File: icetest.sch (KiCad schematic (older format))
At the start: 30 parts

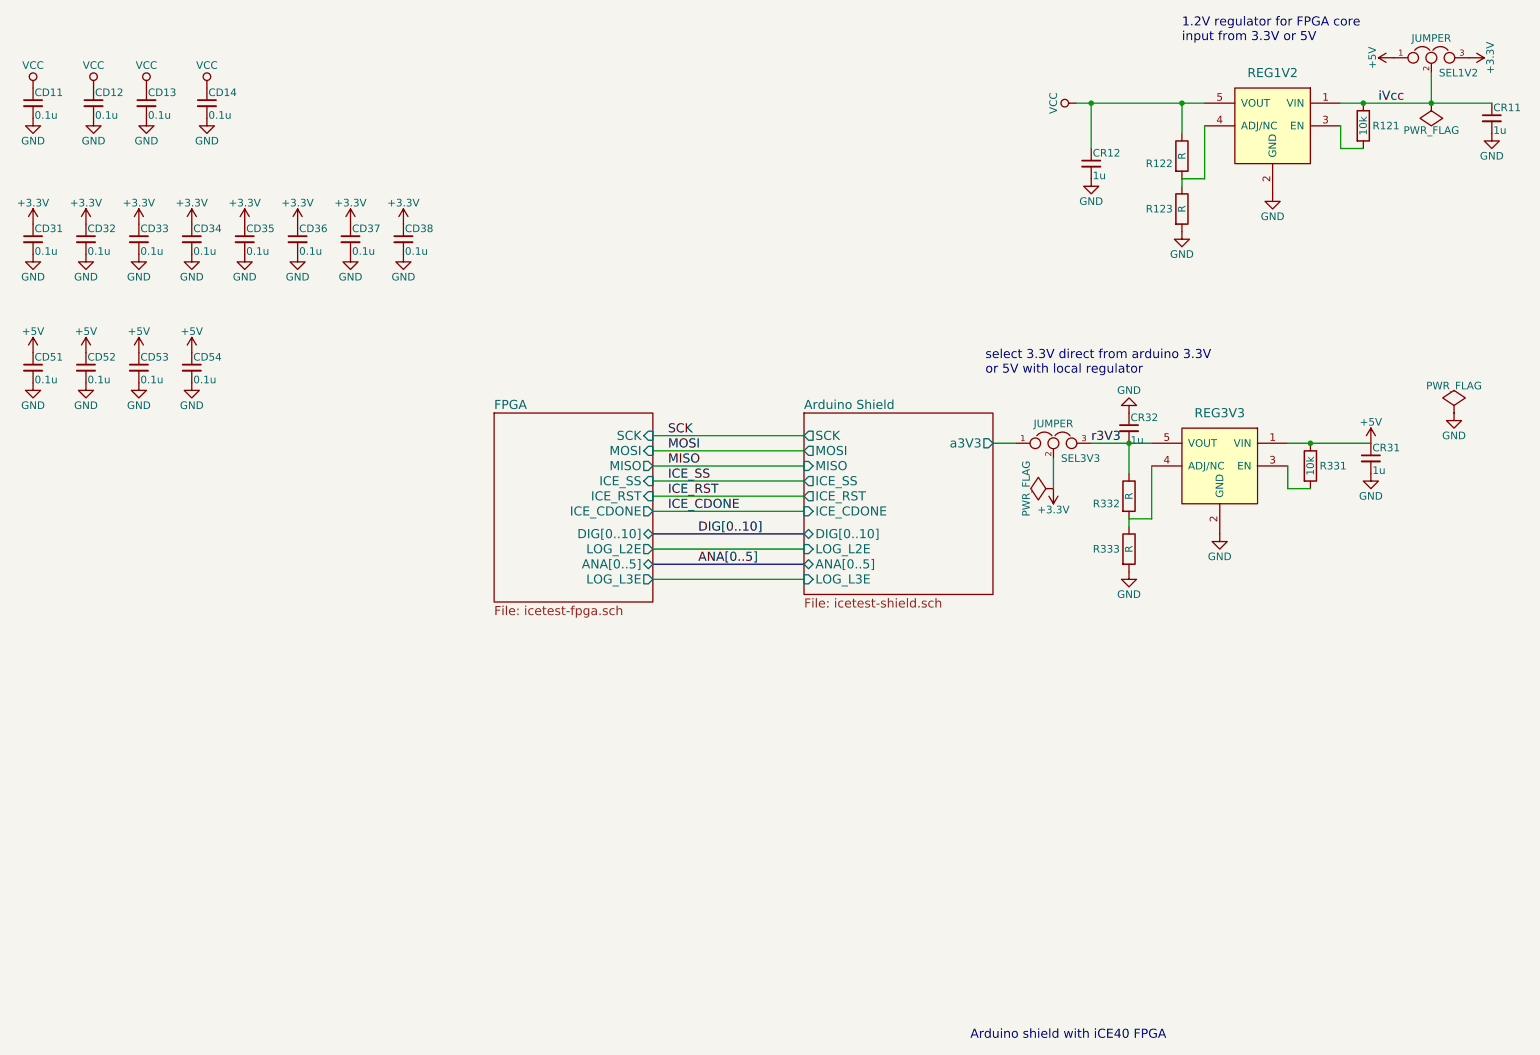
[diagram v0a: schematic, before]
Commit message: add SPI test points and verify footprints
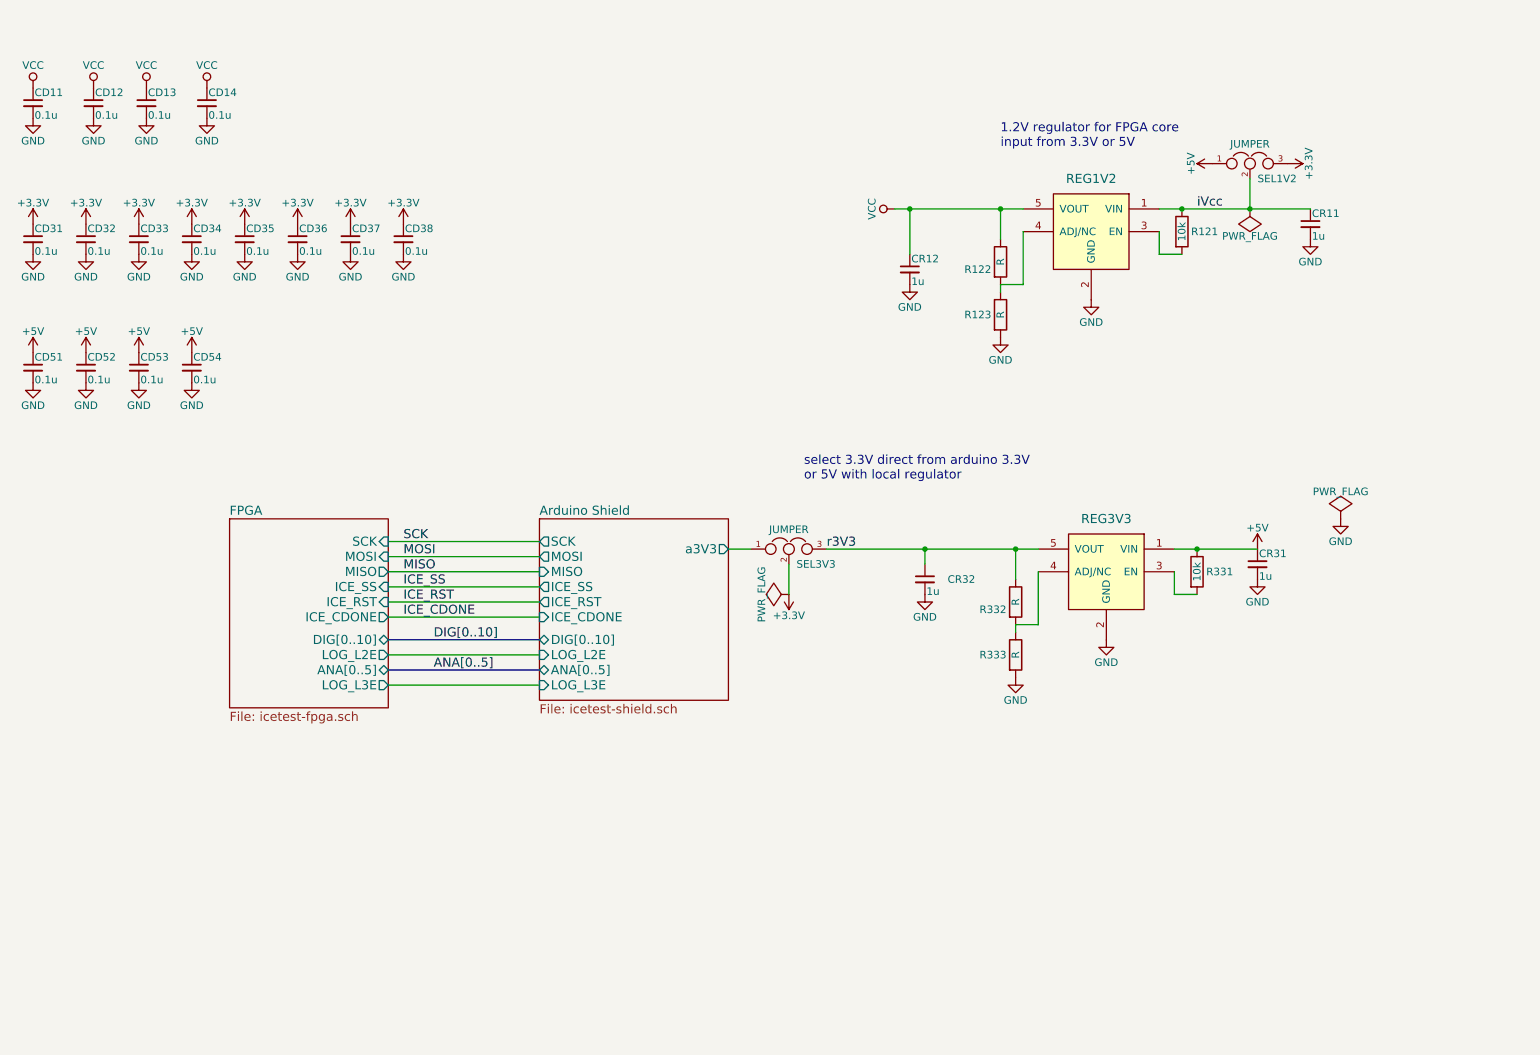
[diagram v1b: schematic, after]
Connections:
- net GND: now also CR32.2; no longer CR32.1
- net r3V3: now also CR32.1; no longer CR32.2
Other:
- note removed: "Arduino shield with iCE40 FPGA"
- moved on the sheet: CR11, CR12, CR31, R121, R122, R123, R331, R332, R333, REG1V2, REG3V3, SEL1V2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

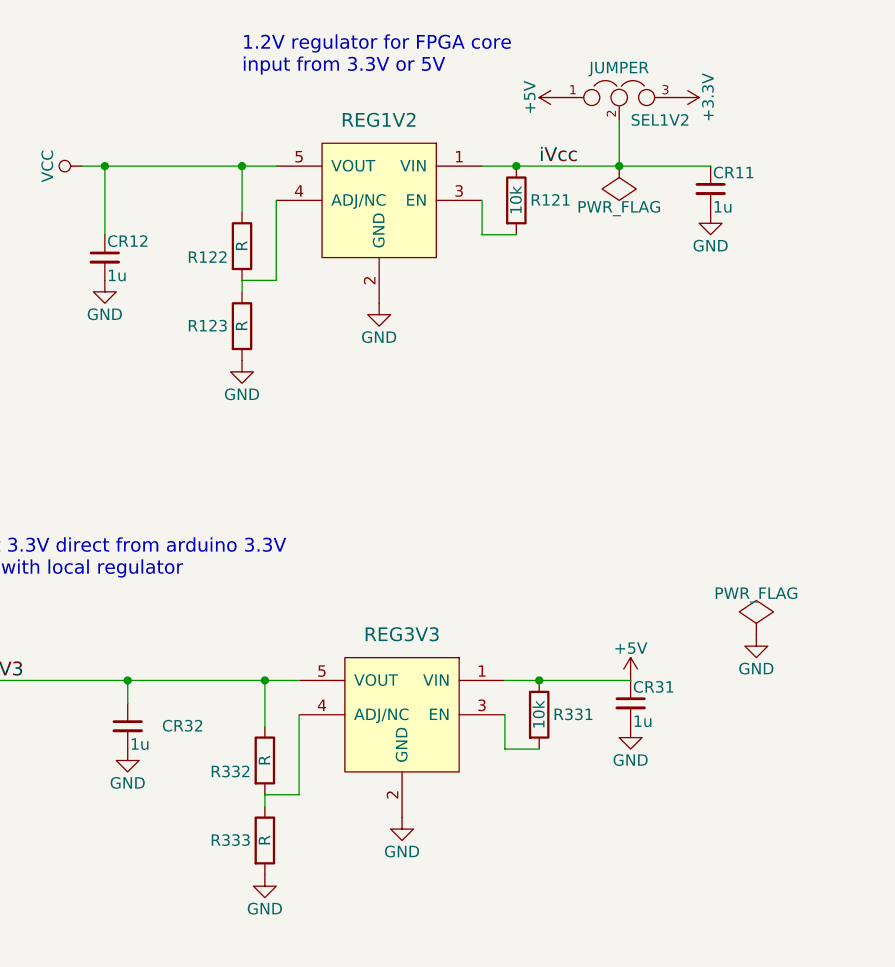
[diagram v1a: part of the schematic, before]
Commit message: fix schematic bugs
signal on N/C pin on ice40
1.2V regulator R divider moved to input side
Remove R divider for 3.3V (not needed for fixed V model)
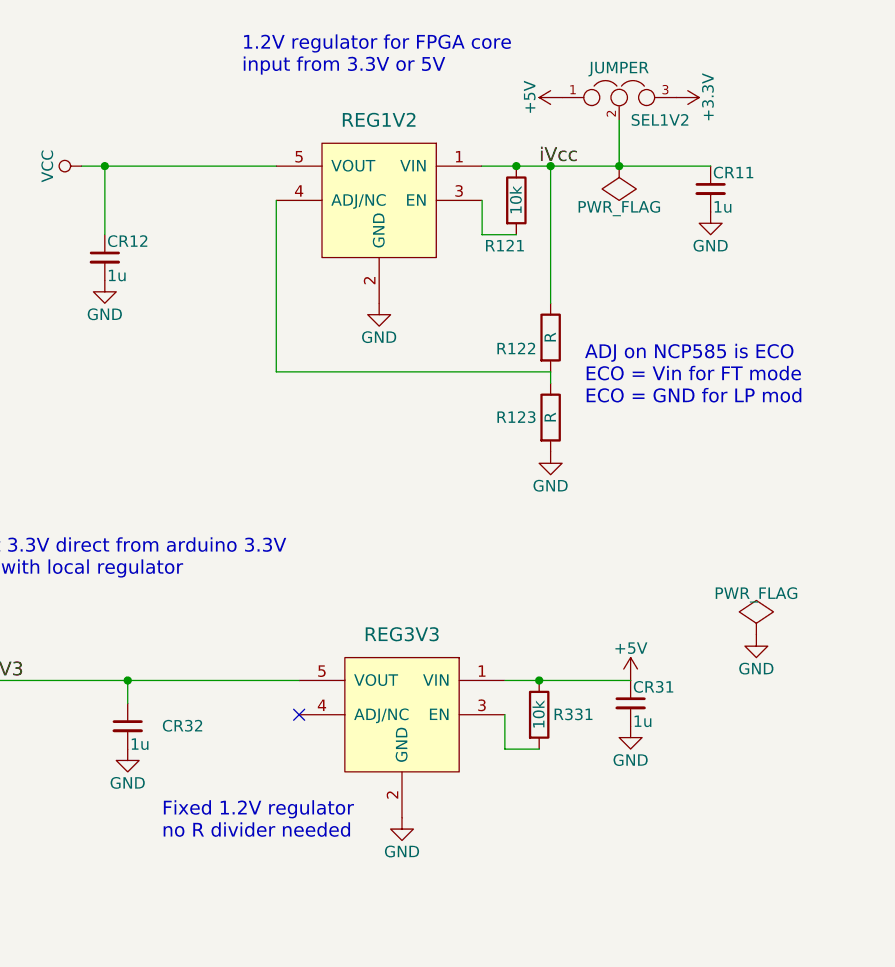
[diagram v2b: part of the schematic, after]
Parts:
- removed R332, R333: R, Resistors_SMD:R_0603_HandSoldering, symbol R
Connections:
- net VCC: no longer R122.1
- net iVcc: now also R122.1
- no-connect marks 0 -> 1
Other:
- note added: "ADJ on NCP585 is ECO\nECO = Vin for FT mode\nECO = GND for LP mod"
- note added: "Fixed 1.2V regulator\nno R divider needed"
- moved on the sheet: R122, R123

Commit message: clean and oshpart rules
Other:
- note added: "Both regulators have\nactive high enable"
- note added: "Fixed 3.3V regulator\nno R divider needed"
- note removed: "Fixed 1.2V regulator\nno R divider needed"
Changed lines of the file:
@@
 NoConn ~ 7850 4400
 Text Notes 7250 4950 0    60   ~ 0
-Fixed 1.2V regulator\nno R divider needed
+Fixed 3.3V regulator\nno R divider needed
+Text Notes 8450 3750 0    60   ~ 0
+Both regulators have\nactive high enable
 $EndSCHEMATC

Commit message: add schematic notes
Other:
- note added: "I/O interconnects\nas 3.3v"
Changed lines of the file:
@@
 Text Notes 8450 3750 0    60   ~ 0
 Both regulators have\nactive high enable
+Text Notes 3650 5550 0    60   ~ 0
+I/O interconnects\nas 3.3v
 $EndSCHEMATC

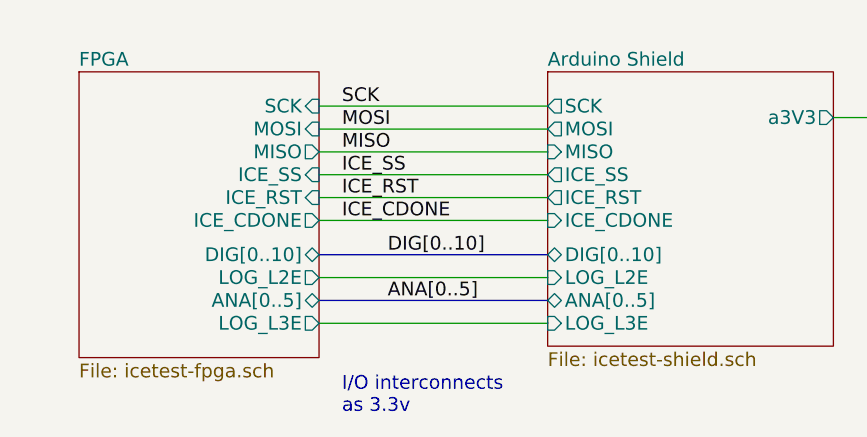
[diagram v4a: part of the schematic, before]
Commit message: switch level shifter
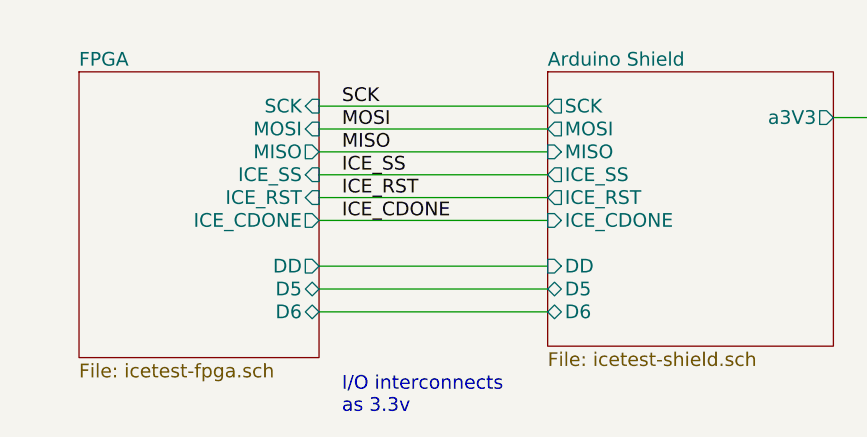
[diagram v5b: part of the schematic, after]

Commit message: redo layout
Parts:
- added W12: TEST_1P, Connect:PINTST, symbol TEST_1P
- SEL1V2, SEL3V3: footprint Connect:PINHEAD1-3 -> Pin_Headers:Pin_Header_Straight_1x03
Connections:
- net VCC: now also W12.1
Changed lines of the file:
@@
 Title "Arduino shield with iCE40 FPGA"
 Date ""
-Rev "0"
+Rev "2"
 Comp "mdavidsaver@gmail.com"
 Comment1 ""
@@
 F 0 "SEL3V3" H 6250 4150 50  0000 L CNN
 F 1 "JUMPER" H 6200 4350 50  0000 C BNN
-F 2 "Connect:PINHEAD1-3" H 6200 4250 50  0001 C CNN
+F 2 "Pin_Headers:Pin_Header_Straight_1x03" H 6200 4250 50  0001 C CNN
 F 3 "" H 6200 4250 50  0000 C CNN
 	1    6200 4250
@@
 F 0 "SEL1V2" H 9300 1600 50  0000 L CNN
 F 1 "JUMPER" H 9250 1800 50  0000 C BNN
-F 2 "Connect:PINHEAD1-3" H 9250 1700 50  0001 C CNN
+F 2 "Pin_Headers:Pin_Header_Straight_1x03" H 9250 1700 50  0001 C CNN
 F 3 "" H 9250 1700 50  0000 C CNN
 	1    9250 1700
@@
 Wire Wire Line
 	3550 5100 4550 5100
+$Comp
+L TEST_1P W12
+U 1 1 57FAF380
+P 7000 2000
+F 0 "W12" H 7000 2270 50  0000 C CNN
+F 1 "TEST_1P" H 7000 2200 50  0000 C CNN
+F 2 "Connect:PINTST" H 7200 2000 50  0001 C CNN
+F 3 "" H 7200 2000 50  0000 C CNN
+	1    7000 2000
+	1    0    0    -1
+$EndComp
 $EndSCHEMATC

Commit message: more layout
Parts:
- added CR4: 1u, Capacitors_SMD:C_0603_HandSoldering, symbol C_Small
- R122, R123: value R -> 10k
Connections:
- net Arduino Shield/a3V3: now also CR4.1
- net GND: now also CR4.2
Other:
- moved on the sheet: SEL3V3
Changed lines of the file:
@@
 L JUMPER3 SEL3V3
 U 1 1 578B8877
-P 6200 4250
-F 0 "SEL3V3" H 6250 4150 50  0000 L CNN
-F 1 "JUMPER" H 6200 4350 50  0000 C BNN
-F 2 "Pin_Headers:Pin_Header_Straight_1x03" H 6200 4250 50  0001 C CNN
-F 3 "" H 6200 4250 50  0000 C CNN
-	1    6200 4250
-	1    0    0    -1
-$EndComp
-Wire Wire Line
-	5950 4250 5800 4250
+P 6500 4250
+F 0 "SEL3V3" H 6550 4150 50  0000 L CNN
+F 1 "JUMPER" H 6500 4350 50  0000 C BNN
+F 2 "Pin_Headers:Pin_Header_Straight_1x03" H 6500 4250 50  0001 C CNN
+F 3 "" H 6500 4250 50  0000 C CNN
+	1    6500 4250
+	1    0    0    -1
+$EndComp
+Wire Wire Line
+	6250 4250 5800 4250
 $Comp
 L +3.3V #PWR01
 U 1 1 578B8957
-P 6200 4550
-F 0 "#PWR01" H 6200 4400 50  0001 C CNN
-F 1 "+3.3V" H 6200 4690 50  0000 C CNN
-F 2 "" H 6200 4550 50  0000 C CNN
-F 3 "" H 6200 4550 50  0000 C CNN
-	1    6200 4550
+P 6500 4550
+F 0 "#PWR01" H 6500 4400 50  0001 C CNN
+F 1 "+3.3V" H 6500 4690 50  0000 C CNN
+F 2 "" H 6500 4550 50  0000 C CNN
+F 3 "" H 6500 4550 50  0000 C CNN
+	1    6500 4550
 	-1   0    0    1
 $EndComp
@@
 $EndComp
 Wire Wire Line
-	6450 4250 7850 4250
+	6750 4250 7850 4250
 $Comp
 L GND #PWR02
@@
 P 8950 2750
 F 0 "R122" H 8800 2700 50  0000 C CNN
-F 1 "R" V 8950 2750 50  0000 C CNN
+F 1 "10k" V 8950 2750 50  0000 C CNN
 F 2 "Resistors_SMD:R_0603_HandSoldering" V 8880 2750 50  0001 C CNN
 F 3 "" H 8950 2750 50  0000 C CNN
@@
 P 8950 3100
 F 0 "R123" H 8800 3100 50  0000 C CNN
-F 1 "R" V 8950 3100 50  0000 C CNN
+F 1 "10k" V 8950 3100 50  0000 C CNN
 F 2 "Resistors_SMD:R_0603_HandSoldering" V 8880 3100 50  0001 C CNN
 F 3 "" H 8950 3100 50  0000 C CNN
@@
 L PWR_FLAG #FLG010
 U 1 1 578BFB2E
-P 6200 4550
-F 0 "#FLG010" H 6200 4645 50  0001 C CNN
-F 1 "PWR_FLAG" H 6200 4730 50  0000 C CNN
-F 2 "" H 6200 4550 50  0000 C CNN
-F 3 "" H 6200 4550 50  0000 C CNN
-	1    6200 4550
+P 6500 4550
+F 0 "#FLG010" H 6500 4645 50  0001 C CNN
+F 1 "PWR_FLAG" H 6500 4730 50  0000 C CNN
+F 2 "" H 6500 4550 50  0000 C CNN
+F 3 "" H 6500 4550 50  0000 C CNN
+	1    6500 4550
 	0    -1   -1   0
 $EndComp
@@
 Connection ~ 7000 2000
 Connection ~ 8900 4250
-Text Label 6450 4250 0    60   ~ 0
+Text Label 6750 4250 0    60   ~ 0
 r3V3
 Text Label 8900 2000 0    60   ~ 0
 iVcc
 Wire Wire Line
-	6200 4350 6200 4550
+	6500 4350 6500 4550
 $Comp
 L C_Small CR32
@@
 	1    0    0    -1
 $EndComp
+$Comp
+L C_Small CR4
+U 1 1 57FE0606
+P 6000 4500
+F 0 "CR4" H 6050 4600 50  0000 L CNN
+F 1 "1u" H 6010 4420 50  0000 L CNN
+F 2 "Capacitors_SMD:C_0603_HandSoldering" H 6000 4500 50  0001 C CNN
+F 3 "" H 6000 4500 50  0000 C CNN
+	1    6000 4500
+	1    0    0    -1
+$EndComp
+$Comp
+L GND #PWR049
+U 1 1 57FE08C3
+P 6000 4600
+F 0 "#PWR049" H 6000 4350 50  0001 C CNN
+F 1 "GND" H 6000 4450 50  0000 C CNN
+F 2 "" H 6000 4600 50  0000 C CNN
+F 3 "" H 6000 4600 50  0000 C CNN
+	1    6000 4600
+	1    0    0    -1
+$EndComp
+Wire Wire Line
+	6000 4400 6000 4250
+Connection ~ 6000 4250
 $EndSCHEMATC

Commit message: more layout
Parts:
- W12: footprint Connect:PINTST -> Measurement_Points:Measurement_Point_Square-SMD-Pad_Small
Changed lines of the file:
@@
 F 0 "W12" H 7000 2270 50  0000 C CNN
 F 1 "TEST_1P" H 7000 2200 50  0000 C CNN
-F 2 "Connect:PINTST" H 7200 2000 50  0001 C CNN
+F 2 "Measurement_Points:Measurement_Point_Square-SMD-Pad_Small" H 7200 2000 50  0001 C CNN
 F 3 "" H 7200 2000 50  0000 C CNN
 	1    7000 2000
